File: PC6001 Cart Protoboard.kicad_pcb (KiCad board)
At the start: 2 copper layers, 97.8 x 80.6 mm, 20 parts, among them J1 PC-6001 edge connector, SW1 PicoReset, SW2 EspReset, SW3 Button A, U2 ESP32-DevKitC, U3 74LS32, U4 microSD-Breakout

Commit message: oopsie on '08
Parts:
- added U5: 74LS08, Package_DIP:DIP-14_W7.62mm_Socket_LongPads, F.Cu at (154.3, 116.2)
- U3: footprint Package_DIP:DIP-14_W7.62mm_LongPads -> Package_DIP:DIP-14_W7.62mm_Socket_LongPads
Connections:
- U3 pad 1: /~{CS3} -> (no net)
- U3 pad 2: /~{CS2} -> (no net)
- U3 pad 3: /~{ROMSEL} -> (no net)
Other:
- board text added: "v1.1 leadedsolder.com 2024"
- board text removed: "v1.0 leadedsolder.com 2024"

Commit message: Rough out locs
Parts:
- moved U2 5.12 mm to (210.4, 106.0)
- moved U1 3.07 mm to (189.9, 80.2)
- moved U3 2.08 mm to (154.0, 137.2)
- moved U5 1.91 mm to (154.3, 118.1)
- moved R1 1.14 mm to (141.0, 121.3)
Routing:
- net /IO0/BUTTON_A: track 169.1 -> 0.00 mm, vias 5 -> 0
- net /ESP_RST: track 108.6 -> 0.00 mm, vias 1 -> 0
- net /a15: track 95.9 -> 0.00 mm, vias 3 -> 0
- net GND: track 94.7 -> 0.00 mm, vias 5 -> 0
- net /IO5/~{SPI_CS}: track 93.7 -> 0.00 mm, vias 3 -> 0
- net /~{ROMSEL}: track 90.2 -> 0.00 mm, vias 1 -> 0
- net /d0: track 82.2 -> 0.00 mm, vias 2 -> 0
- net /~{DRD2}: track 80.8 -> 0.00 mm, vias 3 -> 0
- net /d1: track 80.4 -> 0.00 mm, vias 1 -> 0
- net /ESP_TX: track 79.4 -> 0.00 mm, vias 2 -> 0
- net /a14: track 78.3 -> 0.00 mm, vias 1 -> 0
- net /a11: track 78.2 -> 0.00 mm, vias 1 -> 0
- net /IO19/SPI_MISO: track 77.8 -> 0.00 mm, vias 2 -> 0
- net /a12: track 75.9 -> 0.00 mm, vias 1 -> 0
- net /d2: track 74.6 -> 0.00 mm, vias 2 -> 0
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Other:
- board text added: "TODO: Add some more test hooks for the logic analyzer"
- board text added: "TODO: Place the '08 and '32 properly"

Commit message: Make more room
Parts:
- moved SW2 36.6 mm to (161.6, 70.8)
- moved RN1 32.8 mm to (203.2, 71.8), turned to -90 degrees
- moved SW1 24.5 mm to (172.1, 70.8)
- moved D1 24.5 mm to (182.2, 70.5)
- moved U2 3.83 mm to (210.8, 102.2)
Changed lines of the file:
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@@
 	(footprint "Diode_THT:D_DO-35_SOD27_P7.62mm_Horizontal"
 		(layer "F.Cu")
-		(at 196.215 90.551)
+		(at 182.245 70.485)
 		(descr "Diode, DO-35_SOD27 series, Axial, Horizontal, pin pitch=7.62mm, , length*diameter=4*2mm^2, , http://www.diodes.com/_files/packages/DO-35.pdf")
 		(tags "Diode DO-35_SOD27 series Axial Horizontal pin pitch 7.62mm  length 4mm diameter 2mm")
 		(property "Reference" "D1"
-			(at 3.81 0 0)
+			(at 3.81 0 360)
 			(layer "F.SilkS")
 			(effects
@@
 		)
 		(property "Value" "D"
-			(at 3.81 2.12 0)
+			(at 3.81 2.12 360)
 			(layer "F.Fab")
 			(effects
@@
 		)
 		(fp_text user "K"
-			(at 0 -1.8 0)
+			(at 0 -1.8 360)
 			(layer "F.SilkS")
 			(hide yes)
@@
 		)
 		(fp_text user "${REFERENCE}"
-			(at 4.11 0 0)
+			(at 4.11 0 360)
 			(layer "F.Fab")
 			(effects
@@
 		)
 		(fp_text user "K"
-			(at 0 -1.8 0)
+			(at 0 -1.8 360)
 			(layer "F.Fab")
 			(hide yes)
@@
 		(tags "LED diameter 3.0mm 2 pins")
 		(property "Reference" "D3"
-			(at 1.27 -2.96 0)
+			(at -1.905 0 90)
 			(layer "F.SilkS")
 			(effects
@@
 	(footprint "Button_Switch_THT:SW_PUSH_6mm"
 		(layer "F.Cu")
-		(at 196.469 81.733)
+		(at 161.57 70.775)
 		(descr "Generic 6mm SW tactile push button")
 		(tags "tact sw push 6mm")
 		(property "Reference" "SW2"
-			(at 3.25 -2 0)
+			(at 3.25 2.25 0)
 			(layer "F.SilkS")
 			(effects
@@
 		)
 		(property "Value" "EspReset"
-			(at 3.75 6.7 0)
+			(at 3.25 6.7 0)
 			(layer "F.SilkS")
 			(effects
@@
 	(footprint "Espressif:ESP32-DevKitC"
 		(layer "F.Cu")
-		(at 210.40344 106.045 -90)
+		(at 210.82 102.235 -90)
 		(descr "ESP32-DevKitC: https://docs.espressif.com/projects/esp-idf/en/latest/esp32/hw-reference/esp32/get-started-devkitc.html")
 		(tags "ESP32")
@@
 		)
 		(property "Value" "Button A"
-			(at 3.75 6.7 0)
+			(at 3.25 6.7 0)
 			(layer "F.SilkS")
 			(effects
@@
 	(footprint "Resistor_THT:R_Array_SIP9"
 		(layer "F.Cu")
-		(at 216.027 101.981 180)
+		(at 203.2 71.755 -90)
 		(descr "9-pin Resistor SIP pack")
 		(tags "R")
 		(property "Reference" "RN1"
-			(at 23.622 -0.254 0)
+			(at 23.622 -0.254 90)
 			(layer "F.SilkS")
 			(effects
@@
 		)
 		(property "Value" "10kΩ"
-			(at 11.43 2.4 0)
+			(at 11.43 2.4 90)
 			(layer "F.SilkS")
 			(effects
@@
 		)
 		(property "Footprint" "Resistor_THT:R_Array_SIP9"
-			(at 0 0 180)
+			(at 0 0 -90)
 			(unlocked yes)
 			(layer "F.Fab")
@@
 		)
 		(property "Datasheet" "http://www.vishay.com/docs/31509/csc.pdf"
-			(at 0 0 180)
+			(at 0 0 -90)
 			(unlocked yes)
 			(layer "F.Fab")
@@
 		)
 		(property "Description" "8 resistor network, star topology, bussed resistors, small US symbol"
-			(at 0 0 180)
+			(at 0 0 -90)
 			(unlocked yes)
 			(layer "F.Fab")
@@
 		(attr through_hole)
 		(fp_line
-			(start 21.76 1.4)
-			(end 21.76 -1.4)
+			(start -1.44 1.4)
+			(end 21.76 1.4)
 			(stroke
 				(width 0.12)
@@
 		)
 		(fp_line
-			(start 21.76 -1.4)
-			(end -1.44 -1.4)
+			(start 21.76 1.4)
+			(end 21.76 -1.4)
 			(stroke
 				(width 0.12)
@@
 		)
 		(fp_line
-			(start 1.27 -1.4)
-			(end 1.27 1.4)
+			(start -1.44 -1.4)
+			(end -1.44 1.4)
 			(stroke
 				(width 0.12)
@@
 		)
 		(fp_line
-			(start -1.44 1.4)
-			(end 21.76 1.4)
+			(start 1.27 -1.4)
+			(end 1.27 1.4)
 			(stroke
 				(width 0.12)
@@
 		)
 		(fp_line
-			(start -1.44 -1.4)
-			(end -1.44 1.4)
+			(start 21.76 -1.4)
+			(end -1.44 -1.4)
 			(stroke
 				(width 0.12)
@@
 		)
 		(fp_line
-			(start 22.05 1.65)
-			(end 22.05 -1.65)
+			(start -1.7 1.65)
+			(end 22.05 1.65)
 			(stroke
 				(width 0.05)
@@
 		)
 		(fp_line
-			(start 22.05 -1.65)
-			(end -1.7 -1.65)
+			(start 22.05 1.65)
+			(end 22.05 -1.65)
 			(stroke
 				(width 0.05)
@@
 		)
 		(fp_line
-			(start -1.7 1.65)
-			(end 22.05 1.65)
+			(start -1.7 -1.65)
+			(end -1.7 1.65)
 			(stroke
 				(width 0.05)
@@
 		)
 		(fp_line
-			(start -1.7 -1.65)
-			(end -1.7 1.65)
+			(start 22.05 -1.65)
+			(end -1.7 -1.65)
 			(stroke
 				(width 0.05)
@@
 		)
 		(fp_line
-			(start 21.61 1.25)
-			(end 21.61 -1.25)
+			(start -1.29 1.25)
+			(end 21.61 1.25)
 			(stroke
 				(width 0.1)
@@
 		)
 		(fp_line
-			(start 21.61 -1.25)
-			(end -1.29 -1.25)
+			(start 21.61 1.25)
+			(end 21.61 -1.25)
 			(stroke
 				(width 0.1)
@@
 		)
 		(fp_line
-			(start 1.27 -1.25)
-			(end 1.27 1.25)
+			(start -1.29 -1.25)
+			(end -1.29 1.25)
 			(stroke
 				(width 0.1)
@@
 		)
 		(fp_line
-			(start -1.29 1.25)
-			(end 21.61 1.25)
+			(start 1.27 -1.25)
+			(end 1.27 1.25)
 			(stroke
 				(width 0.1)
@@
 		)
 		(fp_line
-			(start -1.29 -1.25)
-			(end -1.29 1.25)
+			(start 21.61 -1.25)
+			(end -1.29 -1.25)
 			(stroke
 				(width 0.1)
@@
 		)
 		(fp_text user "${REFERENCE}"
-			(at 10.16 0 0)
+			(at 10.16 0 90)
 			(layer "F.Fab")
 			(effects
@@
 		)
 		(pad "1" thru_hole rect
-			(at 0 0 180)
+			(at 0 0 270)
 			(size 1.6 1.6)
 			(drill 0.8)
@@
 		)
 		(pad "2" thru_hole oval
-			(at 2.54 0 180)
+			(at 2.54 0 270)
 			(size 1.6 1.6)
 			(drill 0.8)
@@
 		)
 		(pad "3" thru_hole oval
-			(at 5.08 0 180)
+			(at 5.08 0 270)
 			(size 1.6 1.6)
 			(drill 0.8)
@@
 		)
 		(pad "4" thru_hole oval
-			(at 7.62 0 180)
+			(at 7.62 0 270)
 			(size 1.6 1.6)
 			(drill 0.8)
@@
 		)
 		(pad "5" thru_hole oval
-			(at 10.16 0 180)
+			(at 10.16 0 270)
 			(size 1.6 1.6)
 			(drill 0.8)
@@
 		)
 		(pad "6" thru_hole oval
-			(at 12.7 0 180)
+			(at 12.7 0 270)
 			(size 1.6 1.6)
 			(drill 0.8)
@@
 		)
 		(pad "7" thru_hole oval
-			(at 15.24 0 180)
+			(at 15.24 0 270)
 			(size 1.6 1.6)
 			(drill 0.8)
@@
 		)
 		(pad "8" thru_hole oval
-			(at 17.78 0 180)
+			(at 17.78 0 270)
 			(size 1.6 1.6)
 			(drill 0.8)
@@
 		)
 		(pad "9" thru_hole oval
-			(at 20.32 0 180)
+			(at 20.32 0 270)
 			(size 1.6 1.6)
 			(drill 0.8)
@@
 		(tags "LED diameter 3.0mm 2 pins")
 		(property "Reference" "D2"
-			(at 1.27 -2.96 0)
+			(at -1.9 0 90)
 			(layer "F.SilkS")
 			(effects
@@
 	(footprint "Button_Switch_THT:SW_PUSH_6mm"
 		(layer "F.Cu")
-		(at 196.573 71.5)
+		(at 172.085 70.775)
 		(descr "Generic 6mm SW tactile push button")
 		(tags "tact sw push 6mm")
 		(property "Reference" "SW1"
-			(at 3.25 -2 0)
+			(at 3.25 2.25 0)
 			(layer "F.SilkS")
 			(effects
@@
 		)
 		(property "Value" "PicoReset"
-			(at 3.75 6.7 0)
+			(at 3.25 6.7 0)
 			(layer "F.SilkS")
 			(effects

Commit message: More stuff
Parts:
- moved U2 0.64 mm to (211.5, 102.2)
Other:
- board text added: "d0"
- board text added: "d6"
- board text added: "d7"
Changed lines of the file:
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@@
 	(footprint "Espressif:ESP32-DevKitC"
 		(layer "F.Cu")
-		(at 210.82 102.235 -90)
+		(at 211.455 102.235 -90)
 		(descr "ESP32-DevKitC: https://docs.espressif.com/projects/esp-idf/en/latest/esp32/hw-reference/esp32/get-started-devkitc.html")
 		(tags "ESP32")
@@
 		)
 	)
+	(gr_text "d0"
+		(at 187.96 81.915 90)
+		(layer "B.SilkS")
+		(effects
+			(font
+				(size 1 1)
+				(thickness 0.15)
+			)
+			(justify left bottom mirror)
+		)
+	)
+	(gr_text "d6"
+		(at 172.72 81.915 90)
+		(layer "B.SilkS")
+		(effects
+			(font
+				(size 1 1)
+				(thickness 0.15)
+			)
+			(justify left bottom mirror)
+		)
+	)
 	(gr_text "1"
 		(at 134.62 139.7 0)
@@
 	)
 	(gr_text "~{ROMSEL}"
+		(at 190.5 72.39 90)
+		(layer "B.SilkS")
+		(effects
+			(font
+				(size 1 1)
+				(thickness 0.15)
+			)
+			(justify left bottom mirror)
+		)
+	)
+	(gr_text "~{ROMSEL}"
 		(at 160.655 109.855 45)
 		(layer "B.SilkS")
 		(effects
+			(font
+				(size 1 1)
+				(thickness 0.15)
+			)
+			(justify left bottom mirror)
+		)
+	)
+	(gr_text "d7"
+		(at 167.64 81.915 90)
+		(layer "B.SilkS")
+		(effects

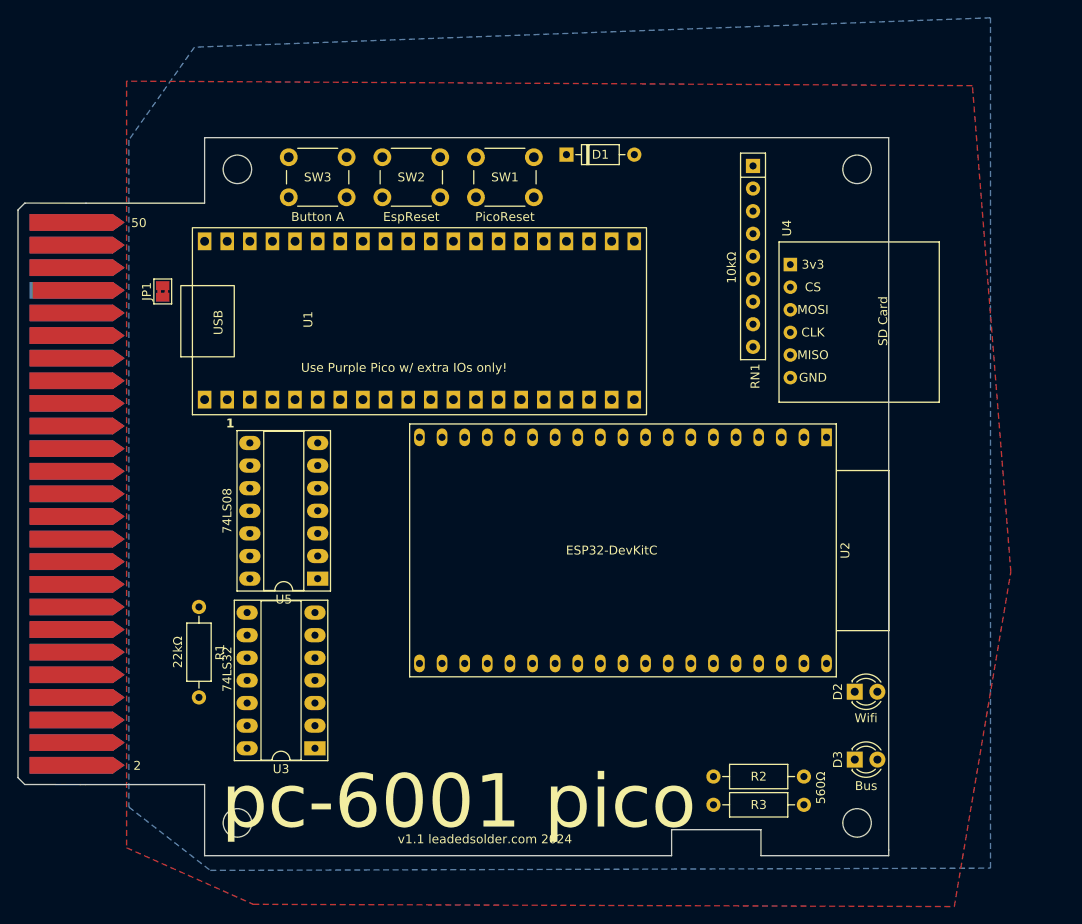
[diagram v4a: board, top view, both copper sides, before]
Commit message: Buffers starting, RAMWR not right
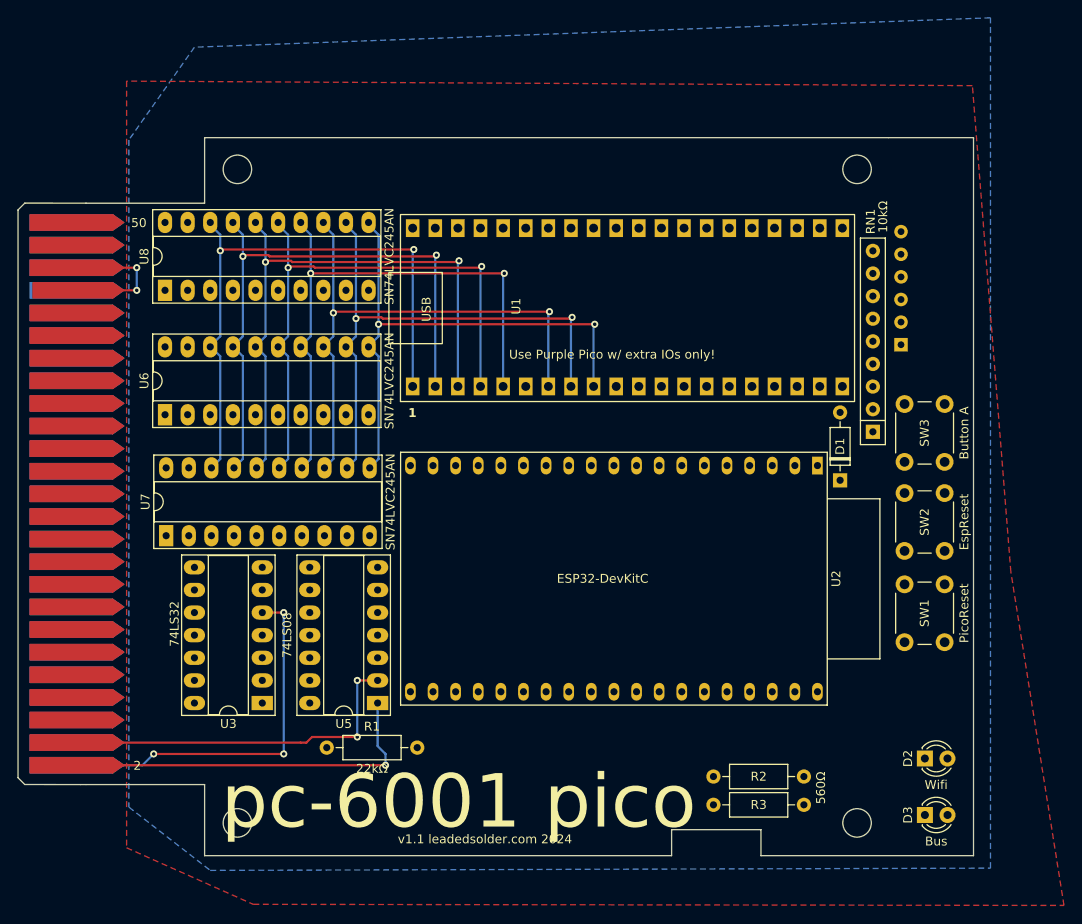
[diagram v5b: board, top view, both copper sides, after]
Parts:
- removed JP1: Jumper_2_Bridged, Jumper:SolderJumper-2_P1.3mm_Bridged2Bar_Pad1.0x1.5mm
- added U6: SN74LVC245AN, Package_DIP:DIP-20_W7.62mm_Socket_LongPads, F.Cu at (137.2, 99.7)
- added U7: SN74LVC245AN, Package_DIP:DIP-20_W7.62mm_Socket_LongPads, F.Cu at (137.3, 113.3)
- added U8: SN74LVC245AN, Package_DIP:DIP-20_W7.62mm_Socket_LongPads, F.Cu at (137.2, 85.7)
- U4: moved to B.Cu
- moved SW3 77.2 mm to (220.2, 105.0), turned to 90 degrees
- moved SW2 73.5 mm to (220.2, 115.0), turned to 90 degrees
- moved SW1 72.7 mm to (220.2, 125.2), turned to 90 degrees
- moved D1 47.8 mm to (213.0, 107.1), turned to 90 degrees
- moved RN1 32.8 mm to (216.7, 101.6), turned to 90 degrees
- moved U1 23.4 mm to (213.2, 78.7)
- moved R1 21.3 mm to (155.3, 137.1), turned to 0 degrees
- moved U4 18.8 mm to (218.6, 94.4), turned to 90 degrees
- moved U5 15.5 mm to (161.0, 132.1)
- moved D2 10.9 mm to (222.5, 138.3)
- moved D3 10.0 mm to (222.5, 144.7)
- moved U3 7.80 mm to (148.1, 132.1)
- moved U2 3.33 mm to (210.4, 105.4)
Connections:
- J1 pad 46: /MSW2 -> /MSW1
- U1 pad 1: /ESP_RX -> /ad0
- U1 pad 10: /a6 -> /~{ROMSEL}
- U1 pad 11: /a7 -> /~{CS3}
- U1 pad 12: /a8 -> /~{WR}
- U1 pad 13: /a9 -> /~{RAMSEL}
- U1 pad 14: /a10 -> /~{WE}
- U1 pad 16: /a11 -> /~{IORQ}
- U1 pad 17: /a12 -> unconnected-(U1-GPIO_14-Pad17)
- U1 pad 18: /a13 -> unconnected-(U1-GPIO_15-Pad18)
- U1 pad 19: /a14 -> unconnected-(U1-GPIO_16-Pad19)
- U1 pad 2: /ESP_TX -> /ad1
- U1 pad 20: /a15 -> unconnected-(U1-GPIO_17-Pad20)
- U1 pad 21: /~{ROMSEL} -> unconnected-(U1-GPIO_18-Pad21)
- U1 pad 22: /d0 -> unconnected-(U1-GPIO_19-Pad22)
- U1 pad 23: /d1 -> unconnected-(U1-GPIO_20-Pad23)
- U1 pad 24: /d2 -> unconnected-(U1-GPIO_21-Pad24)
- U1 pad 25: /d3 -> unconnected-(U1-GPIO_22-Pad25)
- U1 pad 26: /d4 -> unconnected-(U1-GPIO_23-Pad26)
- U1 pad 27: /d5 -> unconnected-(U1-GPIO_24-Pad27)
- U1 pad 28: /d6 -> /ESP_RX
- U1 pad 3: /a0 -> /ad2
- U1 pad 30: /d7 -> /ESP_TX
- U1 pad 4: /a1 -> /ad3
- U1 pad 5: /a2 -> /ad4
- U1 pad 7: /a3 -> /ad5
- U1 pad 8: /a4 -> /ad6
- U1 pad 9: /a5 -> /ad7
- U2 pad 12: /~{RAMSEL} -> unconnected-(U2-MTMS/GPIO14/ADC2_CH6-Pad12)
- U2 pad 13: /~{DRD2} -> unconnected-(U2-MTDI/GPIO12/ADC2_CH5-Pad13)
- U2 pad 15: /~{WR} -> unconnected-(U2-MTCK/GPIO13/ADC2_CH4-Pad15)
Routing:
- net /ad0: track 0.00 -> 66.3 mm, vias 0 -> 2
- net /ad1: track 0.00 -> 65.8 mm, vias 0 -> 2
- net /ad2: track 0.00 -> 65.2 mm, vias 0 -> 2
- net /ad3: track 0.00 -> 64.6 mm, vias 0 -> 2
- net /ad4: track 0.00 -> 63.6 mm, vias 0 -> 2
- net /ad5: track 0.00 -> 61.9 mm, vias 0 -> 2
- net /ad6: track 0.00 -> 61.4 mm, vias 0 -> 2
- net /ad7: track 0.00 -> 60.4 mm, vias 0 -> 2
- net /~{RAS}: track 0.00 -> 45.5 mm, vias 0 -> 3
- net /~{CS3}: track 0.00 -> 45.5 mm, vias 0 -> 1
- net /~{CS2}: track 0.00 -> 43.8 mm, vias 0 -> 2
- net /MSW1: track 0.00 -> 22.9 mm, vias 0 -> 2
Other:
- board size 97.8 x 80.6 mm -> 107.3 x 80.6 mm
- board text added: "ad0"
- board text added: "ad7"
- board text added: "~{RAMCS}"
- board text added: "~{ROMCS}"
- board text removed: "d0"
- board text removed: "d6"
- board text removed: "d7"
- board text removed: "~{RAMSEL}"

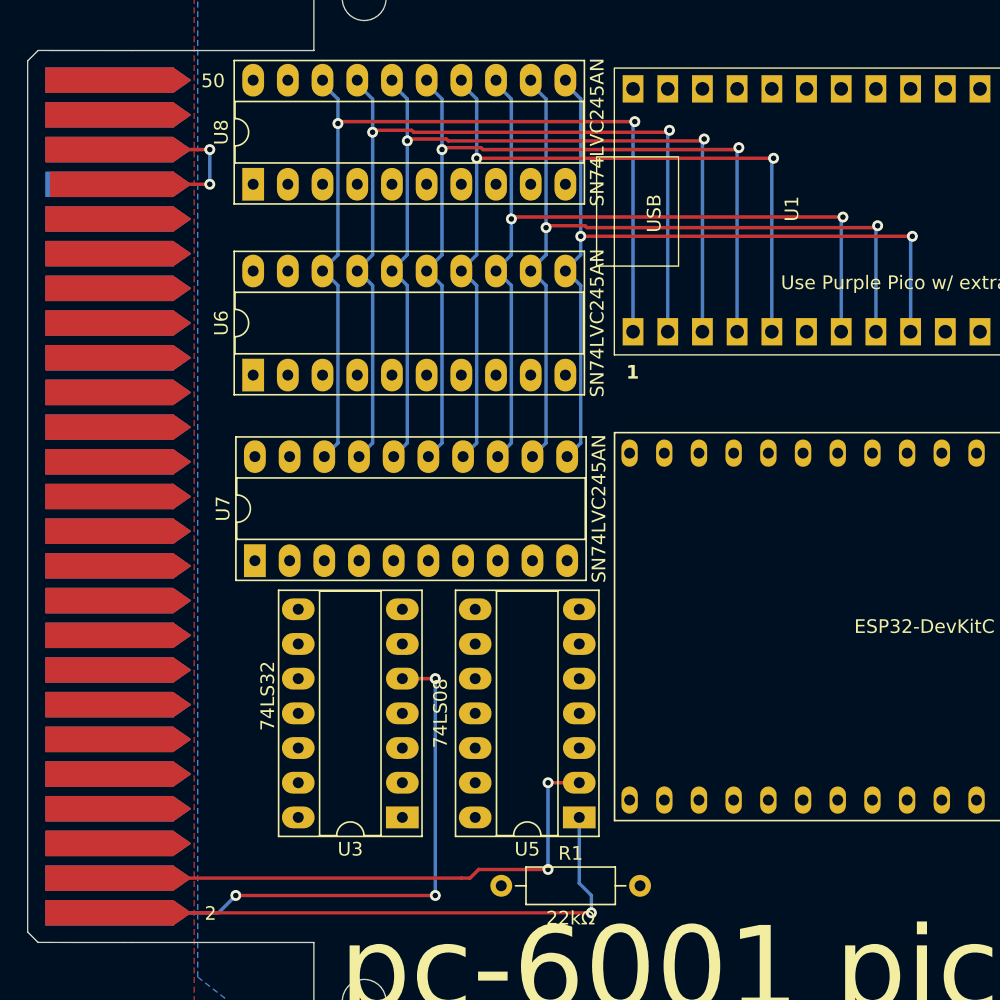
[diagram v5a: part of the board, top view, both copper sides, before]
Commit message: Place nand gate
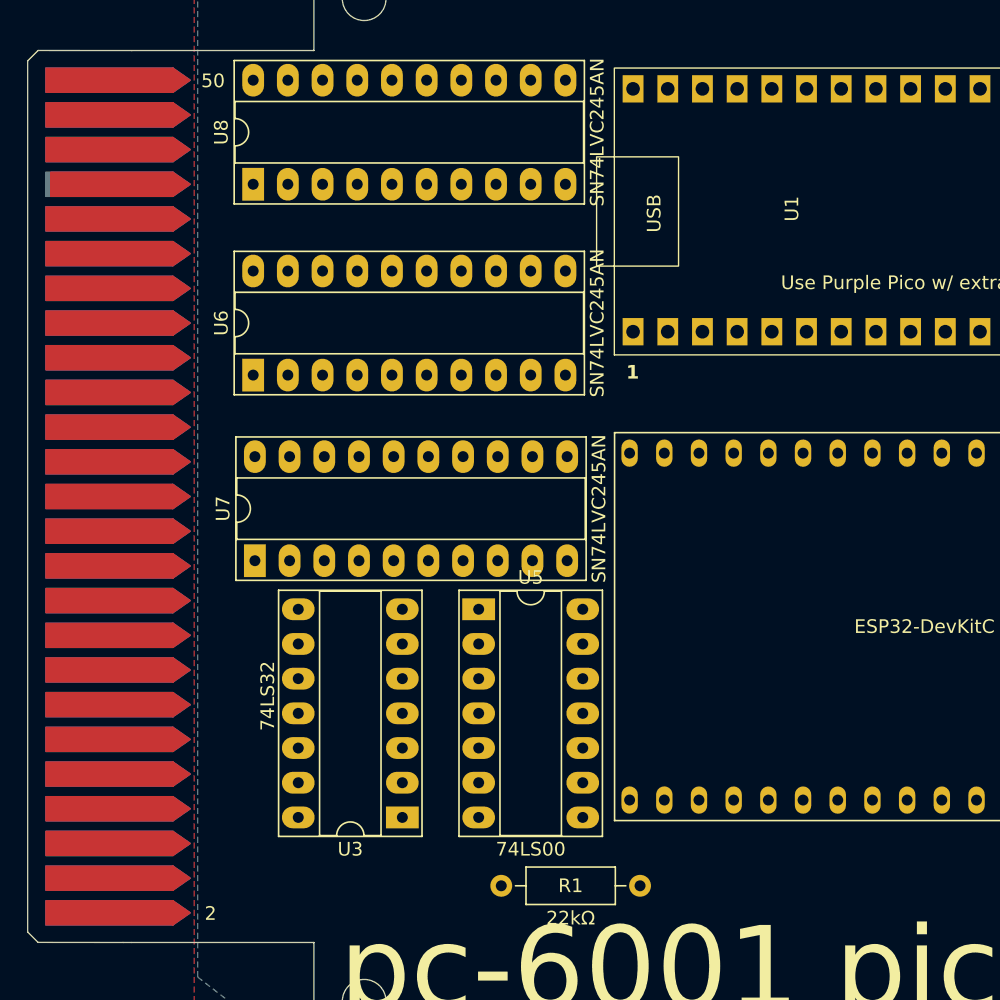
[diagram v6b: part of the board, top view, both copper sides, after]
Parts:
- U5: value 74LS08 -> 74LS00
- moved U5 16.9 mm to (153.7, 116.8), turned to 0 degrees
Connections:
- net /MREQ renamed /~{MREQ}
- J1 pad 11: /IORQ -> /~{IORQ}
- U1 pad 17: unconnected-(U1-GPIO_14-Pad17) -> /~{DRD2}
- U1 pad 23: unconnected-(U1-GPIO_20-Pad23) -> /A/~{D}
- U1 pad 24: unconnected-(U1-GPIO_21-Pad24) -> /H/~{L}
- U1 pad 25: unconnected-(U1-GPIO_22-Pad25) -> /IN/~{OUT}
- U3 pad 1: (no net) -> /H/~{L}
- U3 pad 10: (no net) -> /~{WR}
- U3 pad 11: (no net) -> /~{HI_ADDR}
- U3 pad 12: (no net) -> Net-(U3-Pad12)
- U3 pad 13: (no net) -> /~{ADDR_OE}
- U3 pad 2: (no net) -> /~{ADDR_OE}
- U3 pad 3: (no net) -> /~{LO_ADDR}
- U3 pad 8: (no net) -> /~{IOWR}
- U3 pad 9: (no net) -> /~{IORQ}
- U5 pad 1: /~{CS3} -> /A/~{D}
- U5 pad 10: (no net) -> /~{CS2}
- U5 pad 11: (no net) -> /~{ROMSEL}
- U5 pad 12: (no net) -> Net-(U5-Pad12)
- U5 pad 13: (no net) -> Net-(U5-Pad12)
- U5 pad 2: /~{CS2} -> /A/~{D}
- U5 pad 3: /~{ROMSEL} -> /~{ADDR_OE}
- U5 pad 4: (no net) -> /H/~{L}
- U5 pad 5: (no net) -> /H/~{L}
- U5 pad 6: (no net) -> Net-(U3-Pad12)
- U5 pad 8: (no net) -> Net-(U5-Pad12)
- U5 pad 9: (no net) -> /~{CS3}
- U6 pad 1: unconnected-(U6-DIR-Pad1) -> /IN/~{OUT}
- U6 pad 19: unconnected-(U6-~{OE}-Pad19) -> /~{LO_ADDR}
- U7 pad 1: unconnected-(U7-DIR-Pad1) -> /IN/~{OUT}
- U7 pad 19: unconnected-(U7-~{OE}-Pad19) -> /~{HI_ADDR}
- U8 pad 1: unconnected-(U8-DIR-Pad1) -> /IN/~{OUT}
- U8 pad 19: unconnected-(U8-~{OE}-Pad19) -> /A/~{D}
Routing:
- net /ad0: track 66.3 -> 0.00 mm, vias 2 -> 0
- net /ad1: track 65.8 -> 0.00 mm, vias 2 -> 0
- net /ad2: track 65.2 -> 0.00 mm, vias 2 -> 0
- net /ad3: track 64.6 -> 0.00 mm, vias 2 -> 0
- net /ad4: track 63.6 -> 0.00 mm, vias 2 -> 0
- net /ad5: track 61.9 -> 0.00 mm, vias 2 -> 0
- net /ad6: track 61.4 -> 0.00 mm, vias 2 -> 0
- net /ad7: track 60.4 -> 0.00 mm, vias 2 -> 0
- net /~{RAS}: track 45.5 -> 0.00 mm, vias 3 -> 0
- net /~{CS3}: track 45.5 -> 0.00 mm, vias 1 -> 0
- net /~{CS2}: track 43.8 -> 0.00 mm, vias 2 -> 0
- net /MSW1: track 22.9 -> 0.00 mm, vias 2 -> 0
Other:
- board text removed: "~{ROMCS}"
